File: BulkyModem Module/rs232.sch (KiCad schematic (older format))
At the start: 15 parts, among them J2 DCE, U2 74HCT04, U3 MAX232

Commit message: C64 UserPort adapter sketched out (preliminary layout)
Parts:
- J2: footprint (none) -> RND_DSUB:DSUB-9_Female_Horizontal_P2.77x2.84mm_EdgePinOffset7.70mm_Housed_MountingHolesOffset9.12mm
- JP10, JP11, JP3, JP4, JP5, JP6, JP8, JP9: footprint (none) -> Jumper:SolderJumper-3_P1.3mm_Open_RoundedPad1.0x1.5mm
- U2: footprint (none) -> Package_DIP:DIP-14_W7.62mm_Socket_LongPads
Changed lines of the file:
@@
 F 0 "U2" H 8825 3217 50  0000 C CNN
 F 1 "74HCT04" H 8825 3126 50  0000 C CNN
-F 2 "" H 8825 2900 50  0001 C CNN
+F 2 "Package_DIP:DIP-14_W7.62mm_Socket_LongPads" H 8825 2900 50  0001 C CNN
 F 3 "https://assets.nexperia.com/documents/data-sheet/74HC_HCT04.pdf" H 8825 2900 50  0001 C CNN
 	2    8825 2900
@@
 F 0 "U2" H 8425 4842 50  0000 C CNN
 F 1 "74HCT04" H 8425 4751 50  0000 C CNN
-F 2 "" H 8425 4525 50  0001 C CNN
+F 2 "Package_DIP:DIP-14_W7.62mm_Socket_LongPads" H 8425 4525 50  0001 C CNN
 F 3 "https://assets.nexperia.com/documents/data-sheet/74HC_HCT04.pdf" H 8425 4525 50  0001 C CNN
 	4    8425 4525
@@
 F 0 "U2" H 8450 5467 50  0000 C CNN
 F 1 "74HCT04" H 8450 5376 50  0000 C CNN
-F 2 "" H 8450 5150 50  0001 C CNN
+F 2 "Package_DIP:DIP-14_W7.62mm_Socket_LongPads" H 8450 5150 50  0001 C CNN
 F 3 "https://assets.nexperia.com/documents/data-sheet/74HC_HCT04.pdf" H 8450 5150 50  0001 C CNN
 	5    8450 5150
@@
 F 0 "U2" H 8825 3842 50  0000 C CNN
 F 1 "74HCT04" H 8825 3751 50  0000 C CNN
-F 2 "" H 8825 3525 50  0001 C CNN
+F 2 "Package_DIP:DIP-14_W7.62mm_Socket_LongPads" H 8825 3525 50  0001 C CNN
 F 3 "https://assets.nexperia.com/documents/data-sheet/74HC_HCT04.pdf" H 8825 3525 50  0001 C CNN
 	3    8825 3525
@@
 F 0 "JP8" V 8004 3168 50  0000 L CNN
 F 1 "INV_TX" V 8095 3168 50  0000 L CNN
-F 2 "" H 8050 3100 50  0001 C CNN
+F 2 "Jumper:SolderJumper-3_P1.3mm_Open_RoundedPad1.0x1.5mm" H 8050 3100 50  0001 C CNN
 F 3 "~" H 8050 3100 50  0001 C CNN
 	1    8050 3100
@@
 F 0 "JP9" V 8004 3793 50  0000 L CNN
 F 1 "INV_RTS" V 8095 3793 50  0000 L CNN
-F 2 "" H 8050 3725 50  0001 C CNN
+F 2 "Jumper:SolderJumper-3_P1.3mm_Open_RoundedPad1.0x1.5mm" H 8050 3725 50  0001 C CNN
 F 3 "~" H 8050 3725 50  0001 C CNN
 	1    8050 3725
@@
 F 0 "JP5" H 3750 4450 50  0000 C CNN
 F 1 "CTS_SEL" H 3750 4529 50  0000 C CNN
-F 2 "" H 3750 4325 50  0001 C CNN
+F 2 "Jumper:SolderJumper-3_P1.3mm_Open_RoundedPad1.0x1.5mm" H 3750 4325 50  0001 C CNN
 F 3 "~" H 3750 4325 50  0001 C CNN
 	1    3750 4325
@@
 F 0 "JP6" H 4300 4050 50  0000 C CNN
 F 1 "RTS_SEL" H 4300 4175 50  0000 C CNN
-F 2 "" H 4300 3925 50  0001 C CNN
+F 2 "Jumper:SolderJumper-3_P1.3mm_Open_RoundedPad1.0x1.5mm" H 4300 3925 50  0001 C CNN
 F 3 "~" H 4300 3925 50  0001 C CNN
 	1    4300 3925
@@
 F 0 "JP4" H 3200 3838 50  0000 C CNN
 F 1 "TxD_SEL" H 3200 3929 50  0000 C CNN
-F 2 "" H 3200 3725 50  0001 C CNN
+F 2 "Jumper:SolderJumper-3_P1.3mm_Open_RoundedPad1.0x1.5mm" H 3200 3725 50  0001 C CNN
 F 3 "~" H 3200 3725 50  0001 C CNN
 	1    3200 3725
@@
 F 0 "JP11" V 9271 5017 50  0000 L CNN
 F 1 "INV_CTS" V 9180 5017 50  0000 L CNN
-F 2 "" H 9225 4950 50  0001 C CNN
+F 2 "Jumper:SolderJumper-3_P1.3mm_Open_RoundedPad1.0x1.5mm" H 9225 4950 50  0001 C CNN
 F 3 "~" H 9225 4950 50  0001 C CNN
 	1    9225 4950
@@
 F 0 "JP10" V 9246 4392 50  0000 L CNN
 F 1 "INV_RX" V 9155 4392 50  0000 L CNN
-F 2 "" H 9200 4325 50  0001 C CNN
+F 2 "Jumper:SolderJumper-3_P1.3mm_Open_RoundedPad1.0x1.5mm" H 9200 4325 50  0001 C CNN
 F 3 "~" H 9200 4325 50  0001 C CNN
 	1    9200 4325
@@
 F 0 "J2" H 1913 2417 50  0000 C CNN
 F 1 "DCE" H 1913 2326 50  0000 C CNN
-F 2 "" H 1925 1725 50  0001 C CNN
+F 2 "RND_DSUB:DSUB-9_Female_Horizontal_P2.77x2.84mm_EdgePinOffset7.70mm_Housed_MountingHolesOffset9.12mm" H 1925 1725 50  0001 C CNN
 F 3 " ~" H 1925 1725 50  0001 C CNN
 	1    1925 1725
@@
 F 0 "JP3" H 2650 4250 50  0000 C CNN
 F 1 "RxD_SEL" H 2650 4329 50  0000 C CNN
-F 2 "" H 2650 4125 50  0001 C CNN
+F 2 "Jumper:SolderJumper-3_P1.3mm_Open_RoundedPad1.0x1.5mm" H 2650 4125 50  0001 C CNN
 F 3 "~" H 2650 4125 50  0001 C CNN
 	1    2650 4125

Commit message: Add DCD
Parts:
- added C12, C13, C14, C15: 1uF, BulkyModem:CP_Radial_D4.0mm_P2.00mm_Custom, symbol Device:CP_Small
- added JP12: INV_DCD, Jumper:SolderJumper-3_P1.3mm_Open_RoundedPad1.0x1.5mm, symbol BulkyModem:Swap_Output
- added JP13: NO_DCD, Jumper:SolderJumper-2_P1.3mm_Open_Pad1.0x1.5mm, symbol Jumper:SolderJumper_2_Open
- added unit 6 of U2
- added U4: MAX232, Package_DIP:DIP-16_W7.62mm_Socket_LongPads, symbol Interface_UART:MAX232
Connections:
- net +5V: now also C12.2, U4.16 (VCC)
- net GND: now also C13.1, U4.10 (T2IN), U4.13 (R1IN), U4.15 (GND), U4.8 (R2IN)
- net at J2.4, J2.6: now also JP13.2 (B); no longer J2.1
- new net: JP12.1 (A), U2.12
- new net: JP12.2 (C), U4.11 (T1IN)
- new net: C15.1, U4.1 (C1+)
- new net: C12.1, U4.2 (VS+)
- new net: C15.2, U4.3 (C1-)
- new net: C14.1, U4.4 (C2+)
- new net: C14.2, U4.5 (C2-)
- new net: C13.2, U4.6 (VS-)
- new net 232_DCD: JP12.3 (B), U2.13
- new net SER_DCD: J2.1, JP13.1 (A), U4.14 (T1OUT)
- no-connect marks 1 -> 4
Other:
- note added: "This should be linked if DCD is not available,\nessentially when skipping the installation of\nMAX232 at U4."
- moved on the sheet: C2, C3, C4, C5, J2, JP10, JP11, JP3, JP4, JP5, JP6, JP8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

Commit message: Initial layout
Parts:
- added JP14: INV_RI, Jumper:SolderJumper-3_P1.3mm_Open_RoundedPad1.0x1.5mm, symbol BulkyModem:Swap_Output
- added U5: 74HCT04, Package_DIP:DIP-14_W7.62mm_Socket_LongPads, symbol 74xx:74HCT04
- JP13: value NO_DCD -> BYPASS
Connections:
- net GND: no longer U4.10 (T2IN)
- net SER_RI: now reaches U4.7 (T2OUT)
- net SER_RI: now also J2.9
- new net: JP14.2 (C), U4.10 (T2IN)
- new net: JP14.1 (A), U5.2
- new net 232_RI: JP14.3 (B), U5.1
- no-connect marks 4 -> 2
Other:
- note added: "This should be linked when skipping the\ninstallation of MAX232 at U4."
- note removed: "This should be linked if DCD is not available,\nessentially when skipping the installation of\nMAX232 at U4."
- moved on the sheet: JP12, U2F
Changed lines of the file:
@@
 	-1   0    0    -1
 $EndComp
-NoConn ~ 1600 3225
 Wire Wire Line
 	1600 3325 1675 3325
@@
 L 74xx:74HCT04 U?
 U 6 1 62E77668
-P 8200 1775
+P 8200 1575
 AR Path="/62E77668" Ref="U?"  Part="6"
 AR Path="/6379233A/62E77668" Ref="U2"  Part="6"
-F 0 "U2" H 8200 2092 50  0000 C CNN
-F 1 "74HCT04" H 8200 2001 50  0000 C CNN
-F 2 "Package_DIP:DIP-14_W7.62mm_Socket_LongPads" H 8200 1775 50  0001 C CNN
-F 3 "https://assets.nexperia.com/documents/data-sheet/74HC_HCT04.pdf" H 8200 1775 50  0001 C CNN
-	6    8200 1775
+F 0 "U2" H 8200 1892 50  0000 C CNN
+F 1 "74HCT04" H 8200 1801 50  0000 C CNN
+F 2 "Package_DIP:DIP-14_W7.62mm_Socket_LongPads" H 8200 1575 50  0001 C CNN
+F 3 "https://assets.nexperia.com/documents/data-sheet/74HC_HCT04.pdf" H 8200 1575 50  0001 C CNN
+	6    8200 1575
 	-1   0    0    1
 $EndComp
@@
 L BulkyModem:Swap_Output JP?
 U 1 1 62E8FE3C
-P 7425 1975
+P 7425 1775
 AR Path="/62E8FE3C" Ref="JP?"  Part="1"
 AR Path="/6379233A/62E8FE3C" Ref="JP12"  Part="1"
-F 0 "JP12" V 7379 2043 50  0000 L CNN
-F 1 "INV_DCD" V 7470 2043 50  0000 L CNN
-F 2 "Jumper:SolderJumper-3_P1.3mm_Open_RoundedPad1.0x1.5mm" H 7425 1975 50  0001 C CNN
-F 3 "~" H 7425 1975 50  0001 C CNN
-	1    7425 1975
+F 0 "JP12" V 7379 1843 50  0000 L CNN
+F 1 "INV_DCD" V 7470 1843 50  0000 L CNN
+F 2 "Jumper:SolderJumper-3_P1.3mm_Open_RoundedPad1.0x1.5mm" H 7425 1775 50  0001 C CNN
+F 3 "~" H 7425 1775 50  0001 C CNN
+	1    7425 1775
 	0    1    1    0
 $EndComp
 Wire Wire Line
-	7425 2175 8575 2175
-Wire Wire Line
-	7425 1775 7900 1775
-Wire Wire Line
-	8575 2175 8575 1975
-Wire Wire Line
-	8575 1775 8500 1775
-Wire Wire Line
-	8575 1975 8800 1975
-Connection ~ 8575 1975
+	7425 1975 8575 1975
+Wire Wire Line
+	7425 1575 7900 1575
 Wire Wire Line
 	8575 1975 8575 1775
-Text HLabel 8800 1975 2    50   Input ~ 0
+Wire Wire Line
+	8575 1575 8500 1575
+Wire Wire Line
+	8575 1775 8800 1775
+Connection ~ 8575 1775
+Wire Wire Line
+	8575 1775 8575 1575
+Text HLabel 8800 1775 2    50   Input ~ 0
 232_DCD
 Text Label 4275 1975 0    50   ~ 0
@@
 	-1   0    0    1
 $EndComp
-Wire Wire Line
-	6475 1975 7275 1975
-NoConn ~ 4875 2175
 NoConn ~ 6475 2375
 NoConn ~ 6475 2575
@@
 Wire Wire Line
 	2025 1975 4875 1975
+Wire Wire Line
+	2100 2275 2025 2275
+Connection ~ 2025 2275
+Wire Wire Line
+	2025 2275 2025 1975
+Wire Wire Line
+	1675 2625 2475 2625
+Wire Wire Line
+	2475 2625 2475 2275
+Wire Wire Line
+	2475 2275 2400 2275
+Connection ~ 1675 2625
+Wire Wire Line
+	4700 1775 4875 1775
+Text Notes 2525 2350 0    50   ~ 0
+This should be linked when skipping the\ninstallation of MAX232 at U4.
+Wire Wire Line
+	6475 1975 7075 1975
+Wire Wire Line
+	7075 1975 7075 1775
+Wire Wire Line
+	7075 1775 7275 1775
+Wire Wire Line
+	7075 2175 7075 2375
+Wire Wire Line
+	6475 2175 7075 2175
+$Comp
+L 74xx:74HCT04 U?
+U 1 1 6333079C
+P 8200 2175
+AR Path="/6333079C" Ref="U?"  Part="6"
+AR Path="/6379233A/6333079C" Ref="U5"  Part="1"
+F 0 "U5" H 8200 2492 50  0000 C CNN
+F 1 "74HCT04" H 8200 2401 50  0000 C CNN
+F 2 "Package_DIP:DIP-14_W7.62mm_Socket_LongPads" H 8200 2175 50  0001 C CNN
+F 3 "https://assets.nexperia.com/documents/data-sheet/74HC_HCT04.pdf" H 8200 2175 50  0001 C CNN
+	1    8200 2175
+	-1   0    0    1
+$EndComp
+$Comp
+L BulkyModem:Swap_Output JP?
+U 1 1 633307A2
+P 7425 2375
+AR Path="/633307A2" Ref="JP?"  Part="1"
+AR Path="/6379233A/633307A2" Ref="JP14"  Part="1"
+F 0 "JP14" V 7379 2443 50  0000 L CNN
+F 1 "INV_RI" V 7470 2443 50  0000 L CNN
+F 2 "Jumper:SolderJumper-3_P1.3mm_Open_RoundedPad1.0x1.5mm" H 7425 2375 50  0001 C CNN
+F 3 "~" H 7425 2375 50  0001 C CNN
+	1    7425 2375
+	0    1    1    0
+$EndComp
+Wire Wire Line
+	7425 2575 8575 2575
+Wire Wire Line
+	7425 2175 7900 2175
+Wire Wire Line
+	8575 2575 8575 2375
+Wire Wire Line
+	8575 2175 8500 2175
+Wire Wire Line
+	8575 2375 8800 2375
+Connection ~ 8575 2375
+Wire Wire Line
+	8575 2375 8575 2175
+Text HLabel 8800 2375 2    50   Input ~ 0
+232_RI
+Wire Wire Line
+	7275 2375 7075 2375
+Wire Wire Line
+	1600 3225 4250 3225
+Wire Wire Line
+	4250 3225 4250 2175
+Wire Wire Line
+	4250 2175 4875 2175
+Text Label 4275 2175 0    50   ~ 0
+SER_RI
 $Comp
 L Jumper:SolderJumper_2_Open JP?
@@
 AR Path="/6379233A/62FE8A7C" Ref="JP13"  Part="1"
 F 0 "JP13" H 2250 2436 31  0000 C CNN
-F 1 "NO_DCD" H 2250 2374 31  0000 C CNN
+F 1 "BYPASS" H 2250 2374 31  0000 C CNN
 F 2 "Jumper:SolderJumper-2_P1.3mm_Open_Pad1.0x1.5mm" H 2250 2275 50  0001 C CNN
 F 3 "~" H 2250 2275 50  0001 C CNN
@@
 	1    0    0    -1
 $EndComp
-Wire Wire Line
-	2100 2275 2025 2275
-Connection ~ 2025 2275
-Wire Wire Line
-	2025 2275 2025 1975
-Wire Wire Line
-	1675 2625 2475 2625
-Wire Wire Line
-	2475 2625 2475 2275
-Wire Wire Line
-	2475 2275 2400 2275
-Connection ~ 1675 2625
-Wire Wire Line
-	4700 1775 4875 1775
-Text Notes 2500 2275 0    50   ~ 0
-This should be linked if DCD is not available,\nessentially when skipping the installation of\nMAX232 at U4.
-Wire Wire Line
-	6475 2175 6550 2175
-Wire Wire Line
-	6550 2175 6550 3150
-Wire Wire Line
-	6550 3150 5675 3150
 $EndSCHEMATC

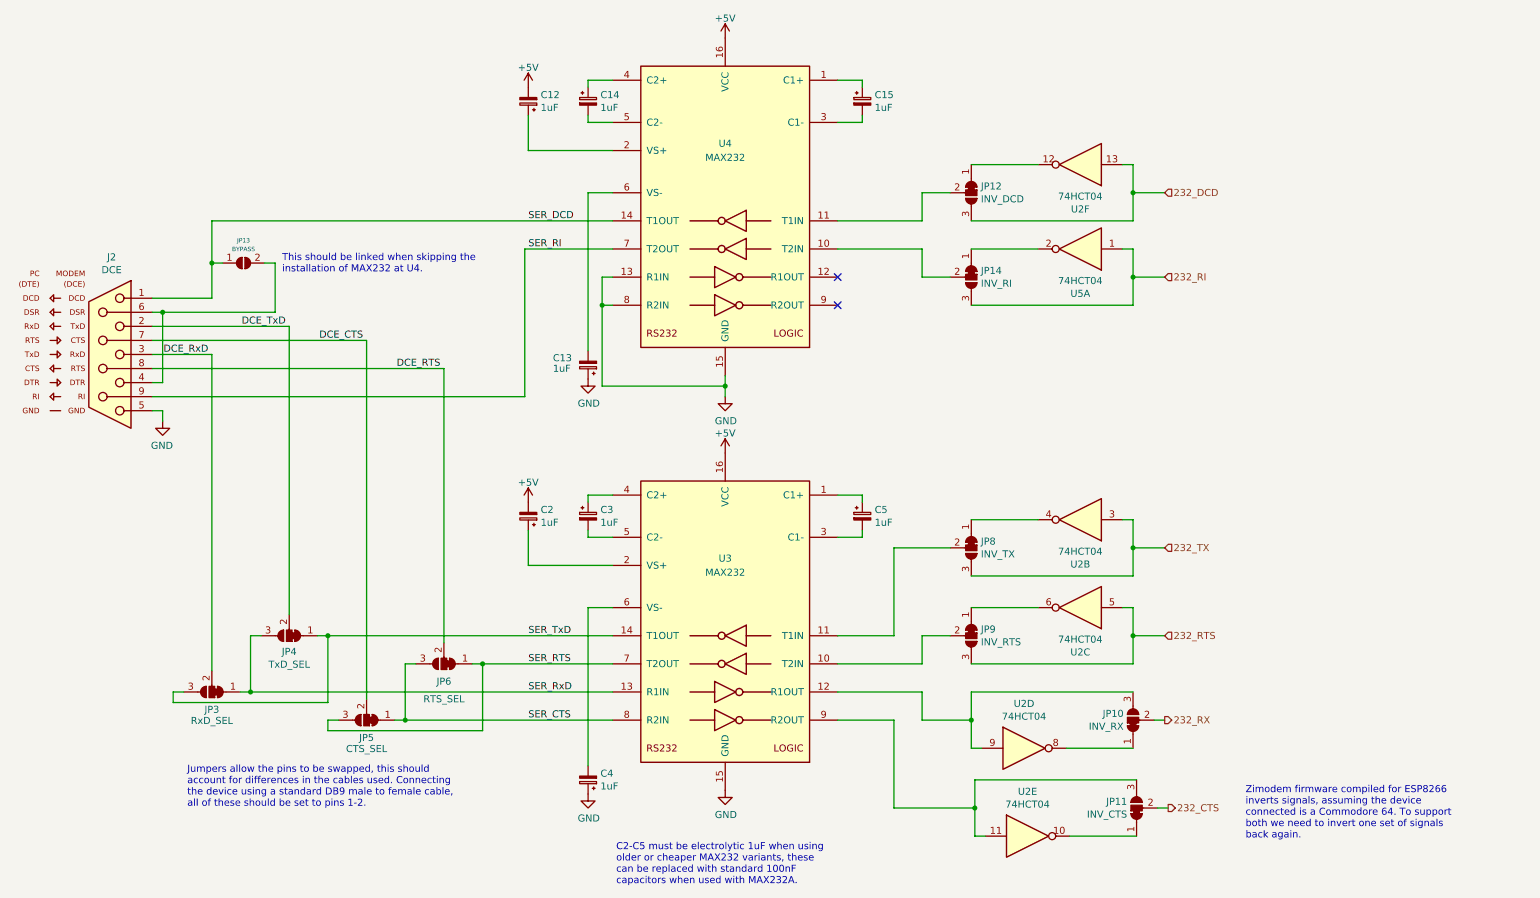
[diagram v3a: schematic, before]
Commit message: Tweak schematic in order to fix LEDs and default jumper settings moved to working configuration
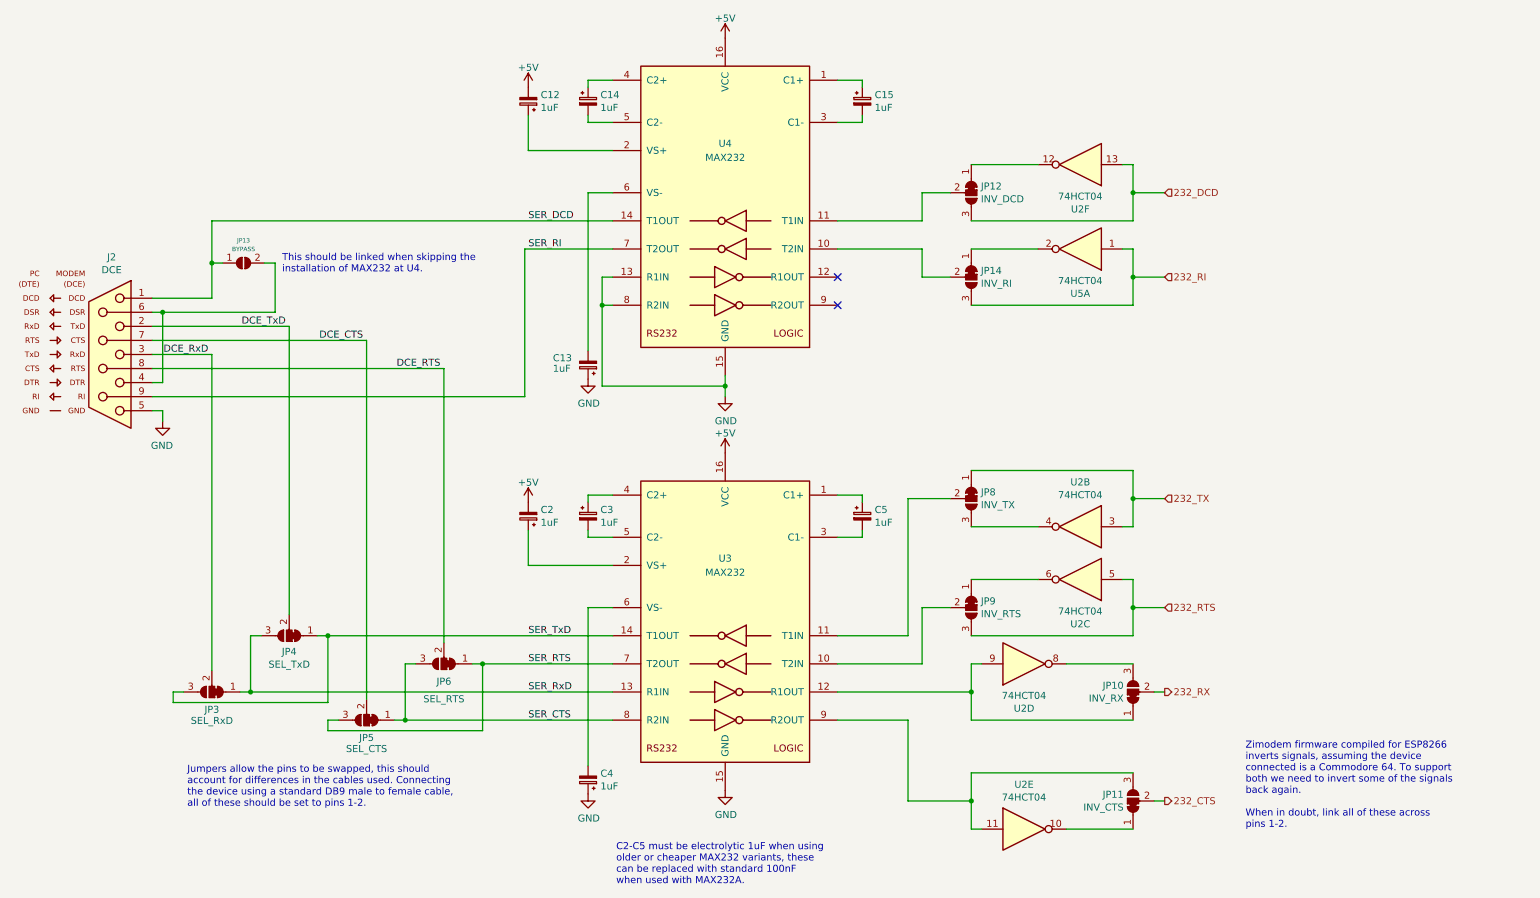
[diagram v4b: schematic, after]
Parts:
- JP3: value RxD_SEL -> SEL_RxD
- JP4: value TxD_SEL -> SEL_TxD
- JP5: value CTS_SEL -> SEL_CTS
- JP6: value RTS_SEL -> SEL_RTS
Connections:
- net 232_TX: now also JP8.1 (A); no longer JP8.3 (B)
- net at U2.4: now also JP8.3 (B); no longer JP8.1 (A)
- net at U2.8: now also JP10.3 (B); no longer JP10.1 (A)
- net at U2.9, U3.12 (R1OUT): now also JP10.1 (A); no longer JP10.3 (B)
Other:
- note added: "C2-C5 must be electrolytic 1uF when using\nolder or cheaper MAX232 variants, these\ncan be replaced with standard 100nF\nwhen used with MAX232A."
- note added: "Zimodem firmware compiled for ESP8266\ninverts signals, assuming the device\nconnected is a Commodore 64. To support\nboth we need to invert some of the signals\nback again.\n\nWhen in doubt, link all of these across\npins 1-2."
- note removed: "C2-C5 must be electrolytic 1uF when using\nolder or cheaper MAX232 variants, these\ncan be replaced with standard 100nF\ncapacitors when used with MAX232A."
- note removed: "Zimodem firmware compiled for ESP8266\ninverts signals, assuming the device\nconnected is a Commodore 64. To support\nboth we need to invert one set of signals\nback again."
- moved on the sheet: JP10, JP11, JP8, JP9, U2B, U2C, U2D, U2E

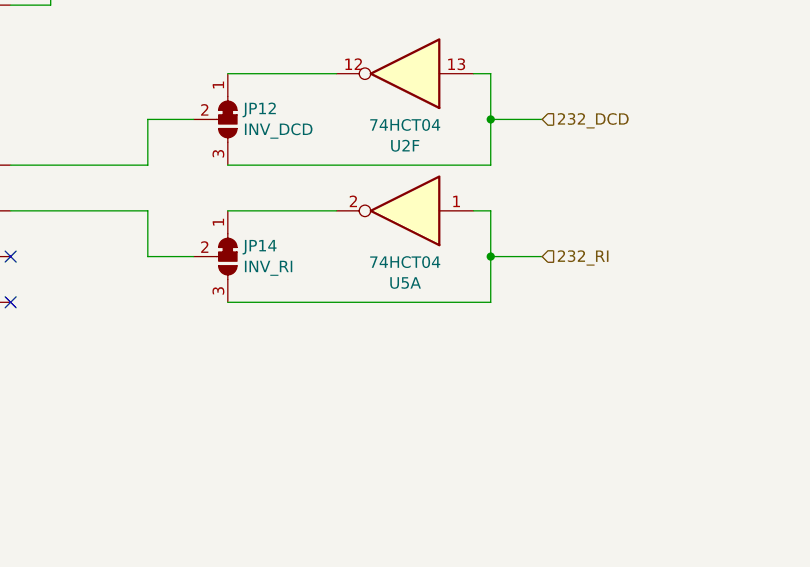
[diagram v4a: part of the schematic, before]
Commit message: Revised version. Mainly buffering signals
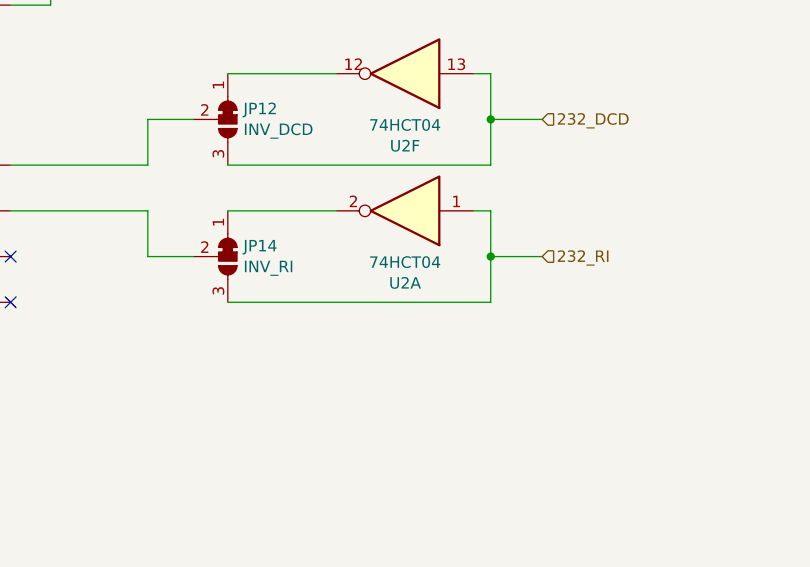
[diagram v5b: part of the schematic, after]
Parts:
- renumbered U5 to U2
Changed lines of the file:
@@
 P 8200 2175
 AR Path="/6333079C" Ref="U?"  Part="6"
-AR Path="/6379233A/6333079C" Ref="U5"  Part="1"
-F 0 "U5" H 8200 2492 50  0000 C CNN
+AR Path="/6379233A/6333079C" Ref="U2"  Part="1"
+F 0 "U2" H 8200 2492 50  0000 C CNN
 F 1 "74HCT04" H 8200 2401 50  0000 C CNN
 F 2 "Package_DIP:DIP-14_W7.62mm_Socket_LongPads" H 8200 2175 50  0001 C CNN
